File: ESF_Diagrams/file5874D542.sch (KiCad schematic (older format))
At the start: 9 parts

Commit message: ESF Fixes
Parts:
- added BT66: Battery, symbol Battery
- added F14: Fuse, symbol Fuse_Small
- added RL1: AIR+, symbol Relay-SPST
- added RL2: AIR-, symbol Relay-SPST
- added U13: MC_Left, symbol Generic_1x1
- added U15: VCU, symbol Generic_1x1
- added U16: MC_Right, symbol Generic_1x1
- added U19: HVIL, symbol Generic_1x1
- added U25: AMS, symbol Generic_1x1
- added U26: Precharge, symbol Generic_1x2
- gave numbers to parts that had none: 9
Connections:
- net at U17.~: now also U25.~; no longer U20.~
- net at U23.~: now also U24.~; no longer U17.~
- net at U20.~: now also U16.~; no longer U22.~
- net at U18.~: now also U15.~; no longer U12.~
- net at U14.~: now also U25.~
- net at U21.~: now also U23.~; no longer U18.~
- new net: U13.~, U17.~
- new net: U20.~, U22.~
- new net: U12.~, U15.~
- new net: U14.~, U19.~
- new net: U18.~, U21.~
- new net: U13.~, U16.~
- new net: BT66.2 (-), RL1.14
- new net: RL1.A2, U19.~, U26.~
- new net: F14.1, RL2.11
- new net: RL2.A2, U26.~
- new net: BT66.1 (+), F14.2
- new net GND: RL1.A1, RL2.A1
- new net TS+: RL2.14
- new net TS-: RL1.11
- new net VCU: U26.~

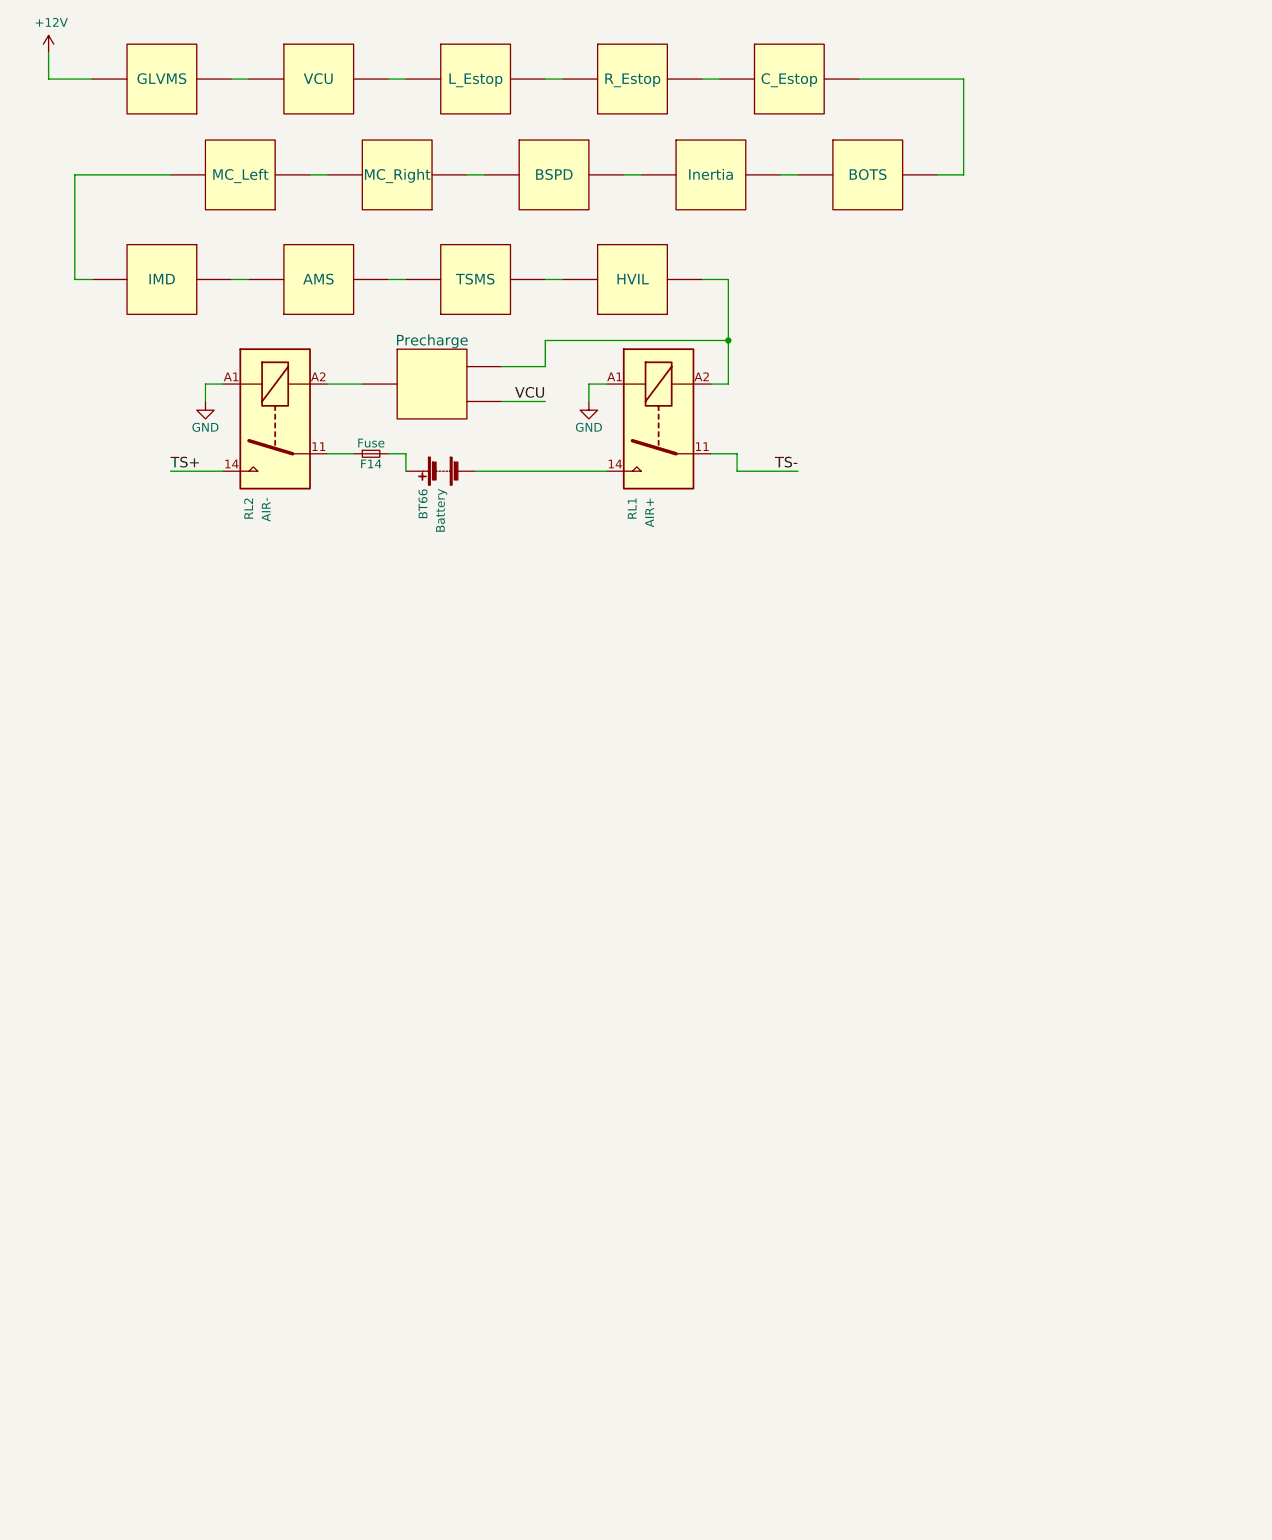
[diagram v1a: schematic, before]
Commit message: Build the Shutdown Circuit in the ESF Diagram
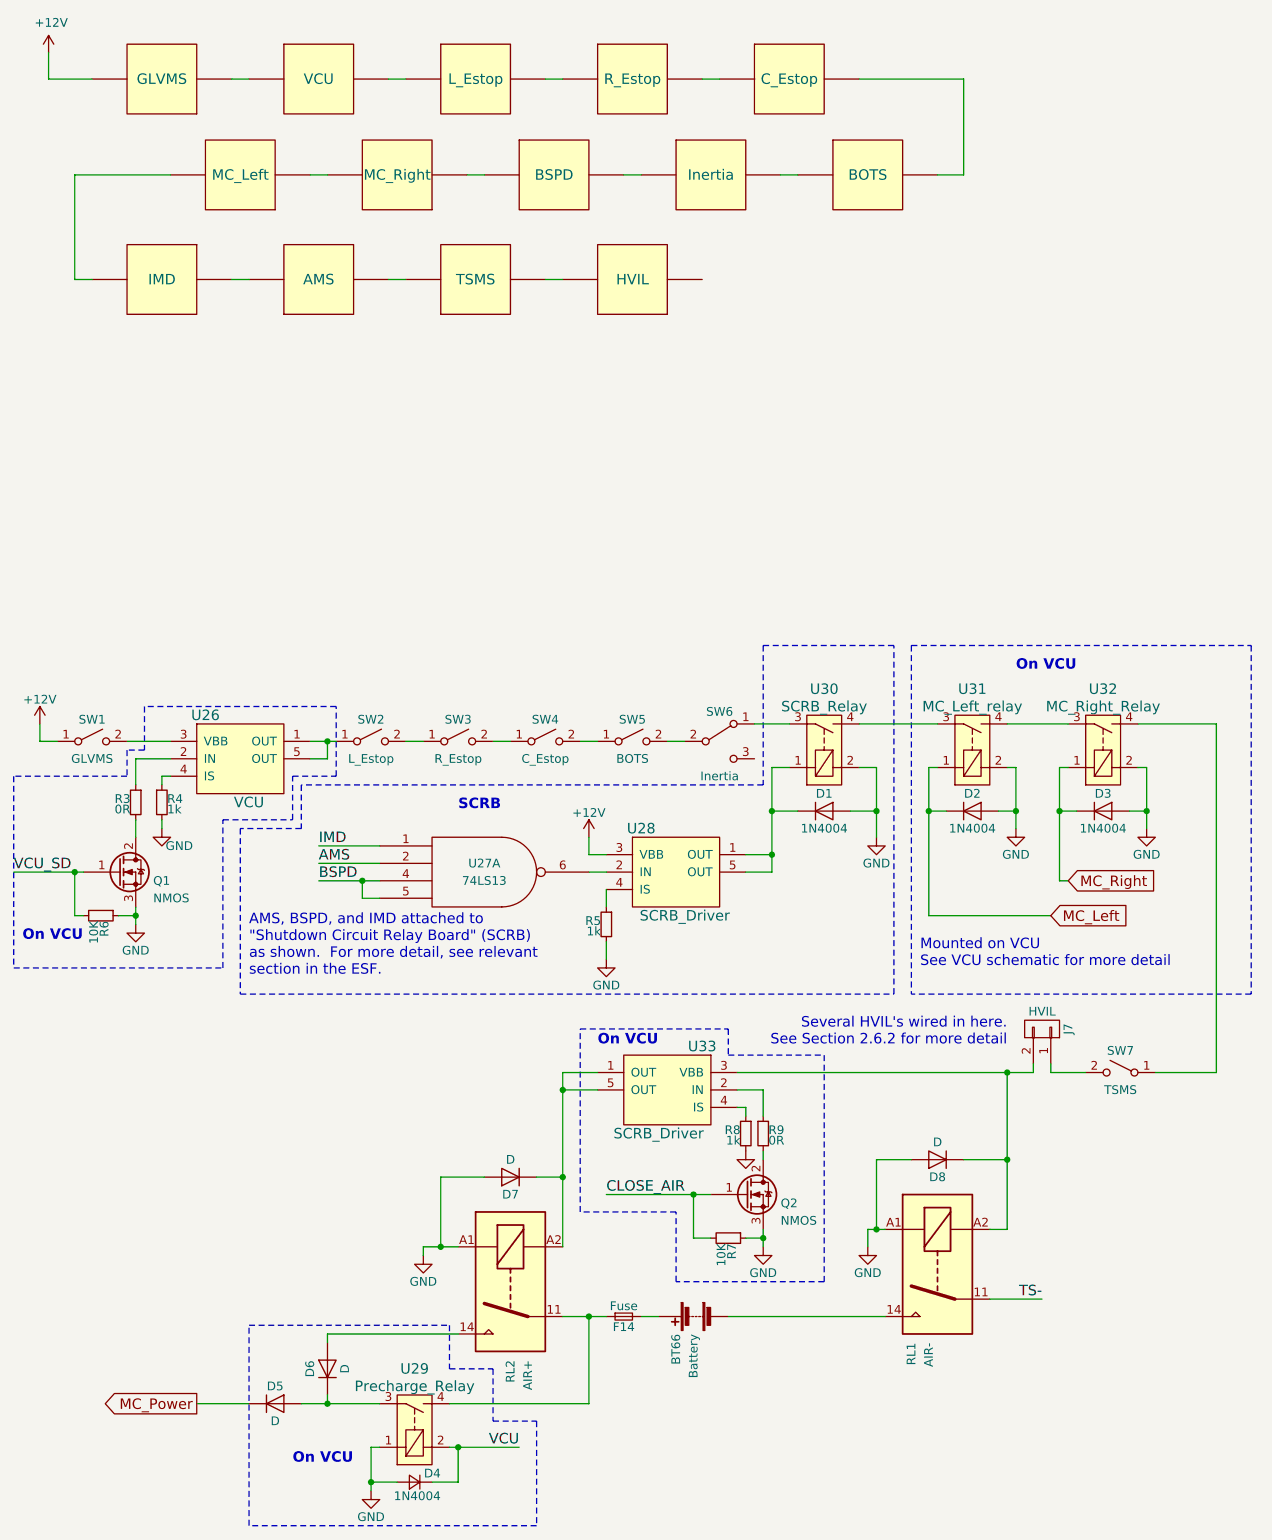
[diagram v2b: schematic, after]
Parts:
- removed U26: Precharge, symbol Generic_1x2
- added D1, D2, D3: 1N4004, symbol D
- added D4: 1N4004, symbol D_Small
- added D5, D6, D7, D8: D, symbol D
- added J7: HVIL, symbol CONN_01X02
- added Q1, Q2: NMOS, symbol Q_NMOS_GDS
- added R3, R9: 0R, symbol R_Small
- added R4, R5, R8: 1k, symbol R_Small
- added R6, R7: 10K, symbol R_Small
- added SW1: GLVMS, symbol SW_SPST
- added SW2: L_Estop, symbol SW_SPST
- added SW3: R_Estop, symbol SW_SPST
- added SW4: C_Estop, symbol SW_SPST
- added SW5: BOTS, symbol SW_SPST
- added SW6: Inertia, symbol SW_SPDT
- added SW7: TSMS, symbol SW_SPST
- added U26: VCU, symbol BTS6133D
- added U27: 74LS13, symbol 74LS13
- added U28, U33: SCRB_Driver, symbol BTS6133D
- added U29: Precharge_Relay, symbol Relay_SPST
- added U30: SCRB_Relay, symbol Relay_SPST
- added U31: MC_Left_relay, symbol Relay_SPST
- added U32: MC_Right_Relay, symbol Relay_SPST
- RL1: value AIR+ -> AIR-
- RL2: value AIR- -> AIR+
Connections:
- net +12V: now also SW1.1 (A), U28.3 (VBB)
- net GND: now also D1.2 (A), D2.2 (A), D3.2 (A), D4.2 (A), D7.2 (A), D8.2 (A), Q1.3 (S), Q2.3 (S), R4.2, R5.2, R6.1, R7.1, R8.2, U27.7 (GND), U29.1, U30.2, U31.2, U32.2
- net VCU: now also D4.1 (K), U29.2
- net at U17.~: now also U25.~; no longer U13.~
- net at U25.~: now also U14.~; no longer U17.~
- net at U20.~: now also U16.~; no longer U22.~
- net at U16.~: now also U13.~; no longer U20.~
- net at U15.~: now also U18.~; no longer U12.~
- net at U19.~: no longer U14.~
- net at U21.~: now also U23.~; no longer U18.~
- net at U23.~: now also U24.~; no longer U21.~
- net at RL1.A2: now also D8.1 (K), J7.2 (P2), U33.3 (VBB); no longer U19.~
- net at F14.1, RL2.11: now also U29.4
- net at RL2.A2: now also D7.1 (K), U33.1 (OUT), U33.5 (OUT)
- net TS+: no longer names the net of RL2.14
- net TS+: now also D6.2 (A)
- new net: U13.~, U17.~
- new net: U20.~, U22.~
- new net: U12.~, U15.~
- new net: U14.~, U19.~
- new net: U18.~, U21.~
- new net: SW1.2 (B), U26.3 (VBB)
- new net: SW2.1 (A), U26.1 (OUT), U26.5 (OUT)
- new net: R3.1, U26.2 (IN)
- new net: R4.1, U26.4 (IS)
- new net: SW2.2 (B), SW3.1 (A)
- new net: SW3.2 (B), SW4.1 (A)
- new net: SW4.2 (B), SW5.1 (A)
- new net: SW5.2 (B), SW6.2 (B)
- new net: SW6.1 (A), U30.3
- new net: Q1.2 (D), R3.2
- new net: U27.6, U28.2 (IN)
- new net: D1.1 (K), U28.1 (OUT), U28.5 (OUT), U30.1
- new net: R5.1, U28.4 (IS)
- new net: SW7.1 (A), U32.4
- new net: J7.1 (P1), SW7.2 (B)
- new net: U30.4, U31.3
- new net: U31.4, U32.3
- new net: D5.2 (A), D6.1 (K), U29.3
- new net: R9.1, U33.2 (IN)
- new net: R8.1, U33.4 (IS)
- new net: Q2.2 (D), R9.2
- new net AMS: U27.2
- new net BSPD: U27.4, U27.5
- new net CLOSE_AIR: Q2.1 (G), R7.2
- new net IMD: U27.1
- new net MC_Left: D2.1 (K), U31.1
- new net MC_Power: D5.1 (K)
- new net MC_Right: D3.1 (K), U32.1
- new net VCC: U27.14 (VCC)
- new net VCU_SD: Q1.1 (G), R6.2
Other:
- note added: "AMS, BSPD, and IMD attached to \n"Shutdown Circuit Relay Board" (SCRB)\nas shown. For more detail, see relevant\nsection in the ESF."
- note added: "Mounted on VCU\nSee VCU schematic for more detail"
- note added: "On VCU"
- note added: "SCRB"
- note added: "Several HVIL's wired in here.\nSee Section 2.6.2 for more detail"
- moved on the sheet: BT66, F14, RL1, RL2

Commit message: Fix error in Precharge Circuit in ESF Diagram
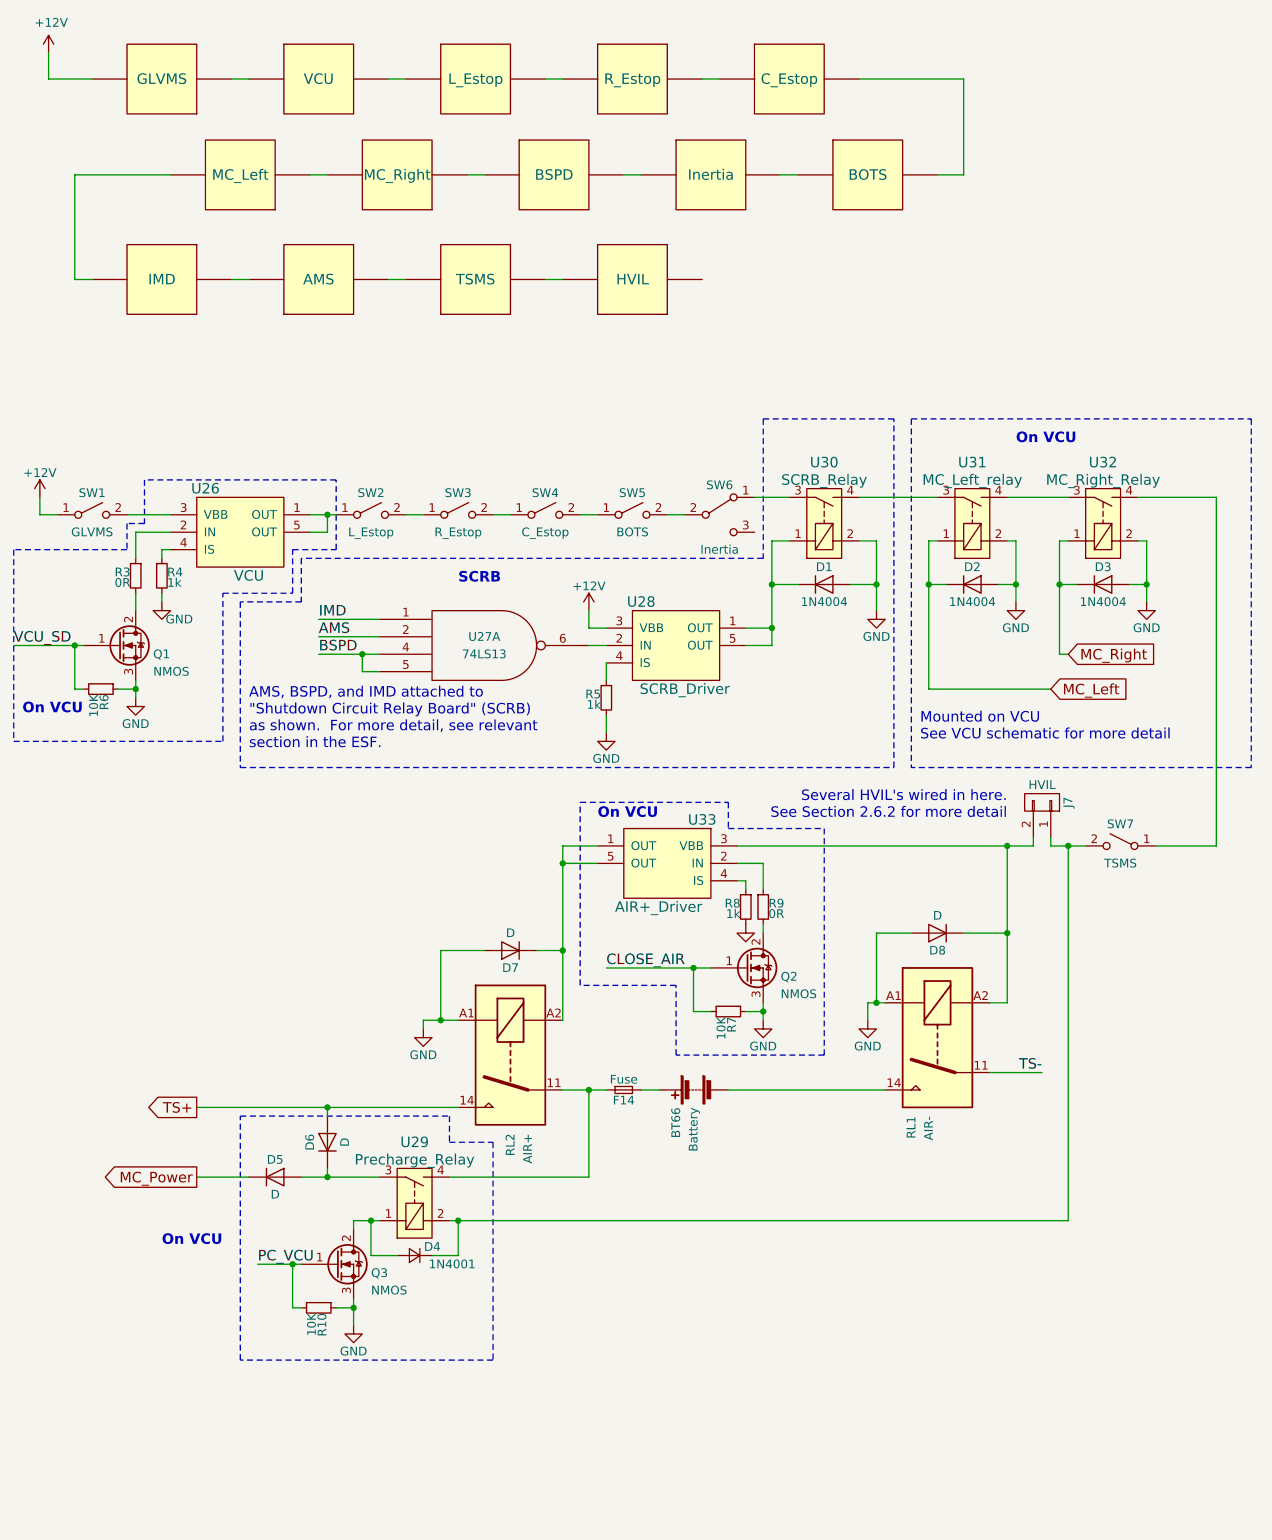
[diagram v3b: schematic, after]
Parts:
- added Q3: NMOS, symbol Q_NMOS_GDS
- added R10: 10K, symbol R_Small
- D4: value 1N4004 -> 1N4001
- U33: value SCRB_Driver -> AIR+_Driver
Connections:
- net VCU is gone; now on an unnamed net: D4.1 (K), U29.2
- net GND: now also Q3.3 (S), R10.1; no longer D4.2 (A), U29.1
- net at U17.~: now also U25.~; no longer U13.~
- net at U25.~: now also U14.~; no longer U17.~
- net at U20.~: now also U16.~; no longer U22.~
- net at U16.~: now also U13.~; no longer U20.~
- net at U15.~: now also U18.~; no longer U12.~
- net at U19.~: no longer U14.~
- net at U21.~: now also U23.~; no longer U18.~
- net at U23.~: now also U24.~; no longer U21.~
- net TS+: now reaches D6.2 (A), RL2.14
- new net: U13.~, U17.~
- new net: U20.~, U22.~
- new net: U12.~, U15.~
- new net: U14.~, U19.~
- new net: U18.~, U21.~
- new net: D4.2 (A), Q3.2 (D), U29.1
- new net PC_VCU: Q3.1 (G), R10.2
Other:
- moved on the sheet: BT66, D1, D2, D3, D4, D5, D6, D7, D8, F14, J7, Q1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
